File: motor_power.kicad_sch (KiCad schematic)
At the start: 11 parts, among them J5 Barrel_Jack_Switch, U4 AP63203WU, U5 TB6612FNG

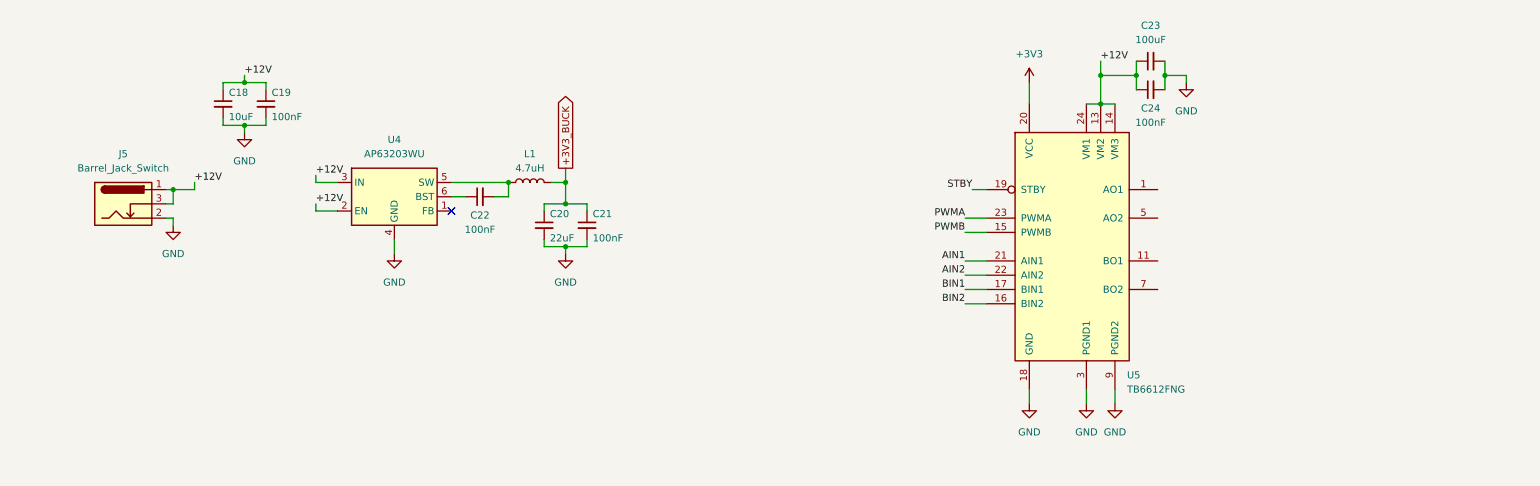
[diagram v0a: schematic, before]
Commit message: connected motor driver
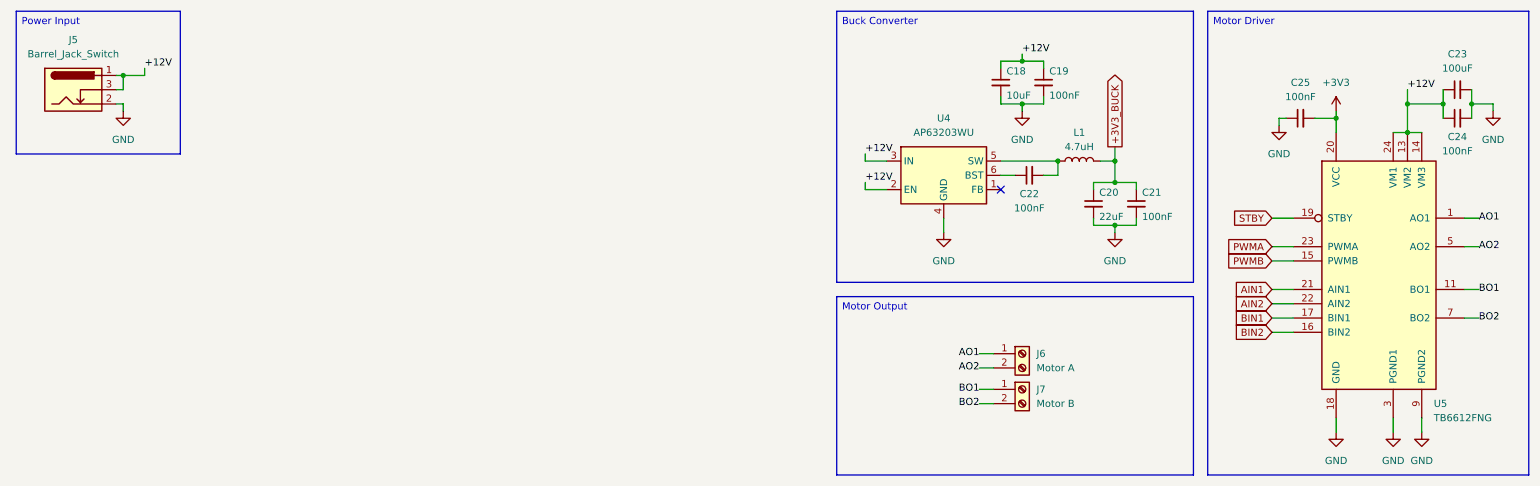
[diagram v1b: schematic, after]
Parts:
- added C25: 100nF, symbol Device:C_Small
- added J6: Motor A, symbol Connector:Screw_Terminal_01x02
- added J7: Motor B, symbol Connector:Screw_Terminal_01x02
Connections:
- net +3V3: now also C25.2
- net GND: now also C25.1
- net AO1: now reaches U5.1 (AO1), U5.2 (AO1)
- net AO1: now also J6.1 (Pin_1)
- net BO1: now reaches U5.11 (BO1), U5.12 (BO1)
- net BO1: now also J7.1 (Pin_1)
- net AO2: now reaches U5.5 (AO2), U5.6 (AO2)
- net AO2: now also J6.2 (Pin_2)
- net BO2: now reaches U5.7 (BO2), U5.8 (BO2)
- net BO2: now also J7.2 (Pin_2)
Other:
- moved on the sheet: C18, C19, C20, C21, C22, C23, C24, J5, L1, U4, U5

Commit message: began working on PCB
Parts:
- C18: footprint (none) -> Capacitor_SMD:C_0603_1608Metric
- C19, C21, C22, C24, C25: footprint (none) -> Capacitor_SMD:C_0402_1005Metric
- C20: footprint (none) -> Capacitor_SMD:C_0805_2012Metric
- C23: footprint (none) -> Capacitor_SMD:C_1206_3216Metric
- J5: footprint (none) -> Connector_BarrelJack:BarrelJack_CUI_PJ-102AH_Horizontal
- J6, J7: footprint (none) -> TerminalBlock:TerminalBlock_MaiXu_MX126-5.0-02P_1x02_P5.00mm
- L1: footprint (none) -> Inductor_SMD:L_0805_2012Metric
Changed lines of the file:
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@@
 			)
 		)
-		(property "Footprint" ""
+		(property "Footprint" "Connector_BarrelJack:BarrelJack_CUI_PJ-102AH_Horizontal"
 			(at 25.4 28.956 0)
 			(hide yes)
@@
 			)
 		)
-		(property "Footprint" ""
+		(property "Footprint" "Capacitor_SMD:C_0402_1005Metric"
 			(at 213.36 48.26 0)
 			(hide yes)
@@
 			)
 		)
-		(property "Footprint" ""
+		(property "Footprint" "Capacitor_SMD:C_1206_3216Metric"
 			(at 270.51 27.94 0)
 			(hide yes)
@@
 			)
 		)
-		(property "Footprint" ""
+		(property "Footprint" "Capacitor_SMD:C_0603_1608Metric"
 			(at 189.23 26.67 0)
 			(hide yes)
@@
 			)
 		)
-		(property "Footprint" ""
+		(property "Footprint" "Capacitor_SMD:C_0402_1005Metric"
 			(at 194.31 43.18 0)
 			(hide yes)
@@
 			)
 		)
-		(property "Footprint" ""
+		(property "Footprint" "Capacitor_SMD:C_0402_1005Metric"
 			(at 196.85 26.67 0)
 			(hide yes)
@@
 			)
 		)
-		(property "Footprint" ""
+		(property "Footprint" "Capacitor_SMD:C_0402_1005Metric"
 			(at 270.51 33.02 0)
 			(hide yes)
@@
 			)
 		)
-		(property "Footprint" ""
+		(property "Footprint" "Capacitor_SMD:C_0805_2012Metric"
 			(at 205.74 48.26 0)
 			(hide yes)
@@
 			)
 		)
-		(property "Footprint" ""
+		(property "Footprint" "Inductor_SMD:L_0805_2012Metric"
 			(at 203.2 40.64 0)
 			(hide yes)
@@
 			)
 		)
-		(property "Footprint" ""
+		(property "Footprint" "TerminalBlock:TerminalBlock_MaiXu_MX126-5.0-02P_1x02_P5.00mm"
 			(at 193.04 81.28 0)
 			(hide yes)
@@
 			)
 		)
-		(property "Footprint" ""
+		(property "Footprint" "Capacitor_SMD:C_0402_1005Metric"
 			(at 242.57 33.02 0)
 			(hide yes)
@@
 			)
 		)
-		(property "Footprint" ""
+		(property "Footprint" "TerminalBlock:TerminalBlock_MaiXu_MX126-5.0-02P_1x02_P5.00mm"
 			(at 193.04 74.93 0)
 			(hide yes)

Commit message: finished first prototype
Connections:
- net STBY is gone; now on net +3V3: U5.19 (STBY)
- net +3V3_BUCK: now also U4.1 (FB)
- no-connect marks 1 -> 0
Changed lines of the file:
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@@
 		(color 0 0 0 0)
 	)
-	(no_connect
-		(at 189.23 45.72)
-	)
 	(wire
 		(pts
@@
 	(wire
 		(pts
+			(xy 234.95 49.53) (xy 234.95 50.8)
+		)
+		(stroke
+			(width 0)
+			(type default)
+		)
+	)
+	(wire
+		(pts
 			(xy 33.02 25.4) (xy 36.83 25.4)
 		)
@@
 	(wire
 		(pts
+			(xy 189.23 45.72) (xy 189.23 46.99)
+		)
+		(stroke
+			(width 0)
+			(type default)
+		)
+	)
+	(wire
+		(pts
 			(xy 33.02 25.4) (xy 33.02 27.94)
 		)
@@
 	(wire
 		(pts
-			(xy 237.49 50.8) (xy 241.3 50.8)
-		)
-		(stroke
-			(width 0)
-			(type default)
-		)
-	)
-	(wire
-		(pts
 			(xy 276.86 30.48) (xy 276.86 31.75)
 		)
@@
 		(pts
 			(xy 205.74 50.8) (xy 205.74 52.07)
+		)
+		(stroke
+			(width 0)
+			(type default)
+		)
+	)
+	(wire
+		(pts
+			(xy 234.95 50.8) (xy 241.3 50.8)
 		)
 		(stroke
@@
 			)
 			(justify left)
-		)
-	)
-	(global_label "STBY"
-		(shape input)
-		(at 237.49 50.8 180)
-		(fields_autoplaced yes)
-		(effects
-			(font
-				(size 1.27 1.27)
-			)
-			(justify right)
-		)
-		(property "Intersheetrefs" "${INTERSHEET_REFS}"
-			(at 229.9691 50.8 0)
-			(hide yes)
-			(show_name no)
-			(do_not_autoplace no)
-			(effects
-				(font
-					(size 1.27 1.27)
-				)
-				(justify right)
-			)
 		)
 	)
@@
 		(property "Intersheetrefs" "${INTERSHEET_REFS}"
 			(at 230.2714 63.5 0)
+			(hide yes)
+			(show_name no)
+			(do_not_autoplace no)
+			(effects
+				(font
+					(size 1.27 1.27)
+				)
+				(justify right)
+			)
+		)
+	)
+	(global_label "+3V3_BUCK"
+		(shape input)
+		(at 189.23 46.99 270)
+		(fields_autoplaced yes)
+		(effects
+			(font
+				(size 1.27 1.27)
+			)
+			(justify right)
+		)
+		(property "Intersheetrefs" "${INTERSHEET_REFS}"
+			(at 189.23 61.1633 90)
 			(hide yes)
 			(show_name no)
@@
 					(unit 1)
 				)
+			)
+		)
+	)
+	(symbol
+		(lib_id "power:+3V3")
+		(at 234.95 49.53 0)
+		(unit 1)
+		(body_style 1)
+		(exclude_from_sim no)
+		(in_bom yes)
+		(on_board yes)
+		(in_pos_files yes)
+		(dnp no)
+		(fields_autoplaced yes)
+		(property "Reference" "#PWR021"
+			(at 234.95 53.34 0)
+			(hide yes)
+			(show_name no)
+			(do_not_autoplace no)
+			(effects
+				(font
+					(size 1.27 1.27)
+				)
+			)
+		)
+		(property "Value" "+3V3"
+			(at 234.95 44.45 0)
+			(show_name no)
+			(do_not_autoplace no)
+			(effects
+				(font
+					(size 1.27 1.27)
+				)
+			)
+		)
+		(property "Footprint" ""
+			(at 234.95 49.53 0)
+			(hide yes)
+			(show_name no)
+			(do_not_autoplace no)
+			(effects
+				(font
+					(size 1.27 1.27)
+				)
+			)
+		)
+		(property "Datasheet" ""
+			(at 234.95 49.53 0)
+			(hide yes)
+			(show_name no)
+			(do_not_autoplace no)
+			(effects
+				(font
+					(size 1.27 1.27)
+				)
+			)
+		)
+		(property "Description" "Power symbol creates a global label with name \"+3V3\""
+			(at 234.95 49.53 0)
+			(hide yes)
+			(show_name no)
+			(do_not_autoplace no)
+			(effects
+				(font
+					(size 1.27 1.27)
+				)
+			)
+		)
+		(pin "1"
+		)
+		(instances
+			(project "devboard"
+				(path "/761eecd5-cc9b-4512-b74d-b293fa8ee57d/516e0ff6-2ca1-4482-bb23-5e8abf72d778"
+					(reference "#PWR021")
+					(unit 1)
+				)
